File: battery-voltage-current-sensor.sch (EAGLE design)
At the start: 66 parts, among them IC1 ACS758LCB-050B-PFF-T, IC3 ADS1115IDGST, T1 C8545, T2 C8545, T3 C8545, X1 MKDSN1,5/2-5,08

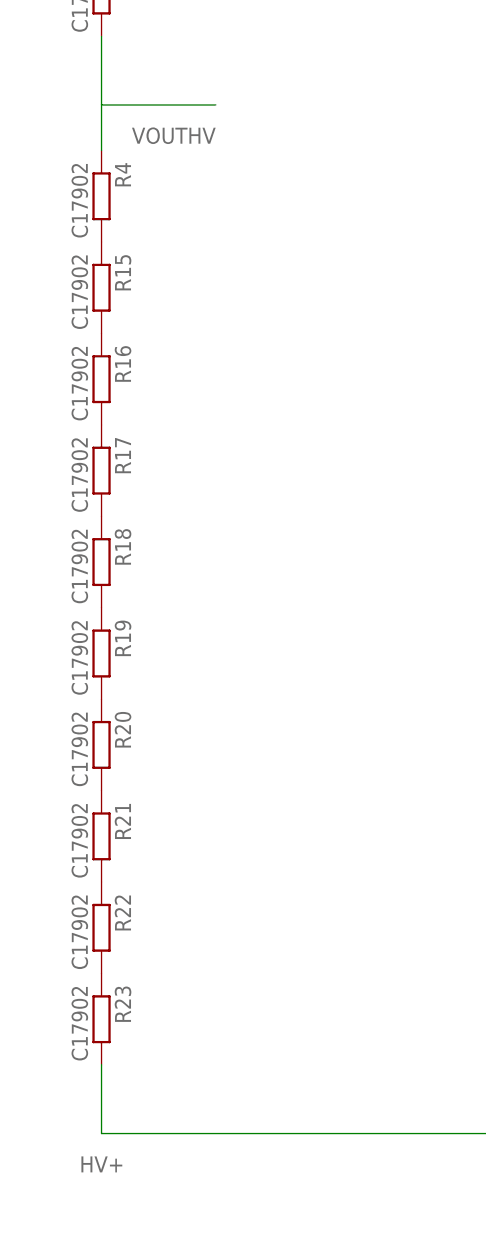
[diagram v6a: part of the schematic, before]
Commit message: voltage measurement resistors changed to 100k
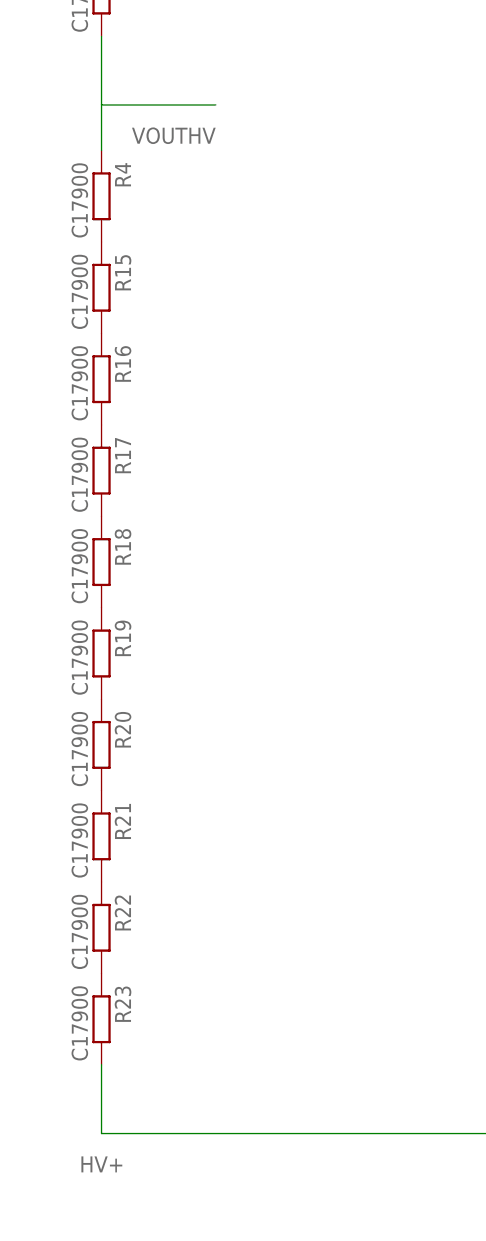
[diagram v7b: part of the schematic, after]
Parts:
- R15, R16, R17, R18, R19, R20, R21, R22, R23, R4: value C17902 -> C17900
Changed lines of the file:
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@@
 <part name="IC1" library="allegro" library_urn="urn:adsk.eagle:library:93" deviceset="ACS758*" device="" package3d_urn="urn:adsk.eagle:package:3449/1" technology="LCB-050B-PFF-T"/>
 <part name="IC3" library="SamacSys_Parts" deviceset="ADS1115IDGST" device=""/>
-<part name="R4" library="rcl" library_urn="urn:adsk.eagle:library:334" deviceset="R-EU_" device="R1206" package3d_urn="urn:adsk.eagle:package:23540/2" value="C17902"/>
-<part name="R15" library="rcl" library_urn="urn:adsk.eagle:library:334" deviceset="R-EU_" device="R1206" package3d_urn="urn:adsk.eagle:package:23540/2" value="C17902"/>
-<part name="R16" library="rcl" library_urn="urn:adsk.eagle:library:334" deviceset="R-EU_" device="R1206" package3d_urn="urn:adsk.eagle:package:23540/2" value="C17902"/>
-<part name="R17" library="rcl" library_urn="urn:adsk.eagle:library:334" deviceset="R-EU_" device="R1206" package3d_urn="urn:adsk.eagle:package:23540/2" value="C17902"/>
-<part name="R18" library="rcl" library_urn="urn:adsk.eagle:library:334" deviceset="R-EU_" device="R1206" package3d_urn="urn:adsk.eagle:package:23540/2" value="C17902"/>
-<part name="R19" library="rcl" library_urn="urn:adsk.eagle:library:334" deviceset="R-EU_" device="R1206" package3d_urn="urn:adsk.eagle:package:23540/2" value="C17902"/>
-<part name="R20" library="rcl" library_urn="urn:adsk.eagle:library:334" deviceset="R-EU_" device="R1206" package3d_urn="urn:adsk.eagle:package:23540/2" value="C17902"/>
-<part name="R21" library="rcl" library_urn="urn:adsk.eagle:library:334" deviceset="R-EU_" device="R1206" package3d_urn="urn:adsk.eagle:package:23540/2" value="C17902"/>
-<part name="R22" library="rcl" library_urn="urn:adsk.eagle:library:334" deviceset="R-EU_" device="R1206" package3d_urn="urn:adsk.eagle:package:23540/2" value="C17902"/>
-<part name="R23" library="rcl" library_urn="urn:adsk.eagle:library:334" deviceset="R-EU_" device="R1206" package3d_urn="urn:adsk.eagle:package:23540/2" value="C17902"/>
+<part name="R4" library="rcl" library_urn="urn:adsk.eagle:library:334" deviceset="R-EU_" device="R1206" package3d_urn="urn:adsk.eagle:package:23540/2" value="C17900"/>
+<part name="R15" library="rcl" library_urn="urn:adsk.eagle:library:334" deviceset="R-EU_" device="R1206" package3d_urn="urn:adsk.eagle:package:23540/2" value="C17900"/>
+<part name="R16" library="rcl" library_urn="urn:adsk.eagle:library:334" deviceset="R-EU_" device="R1206" package3d_urn="urn:adsk.eagle:package:23540/2" value="C17900"/>
+<part name="R17" library="rcl" library_urn="urn:adsk.eagle:library:334" deviceset="R-EU_" device="R1206" package3d_urn="urn:adsk.eagle:package:23540/2" value="C17900"/>
+<part name="R18" library="rcl" library_urn="urn:adsk.eagle:library:334" deviceset="R-EU_" device="R1206" package3d_urn="urn:adsk.eagle:package:23540/2" value="C17900"/>
+<part name="R19" library="rcl" library_urn="urn:adsk.eagle:library:334" deviceset="R-EU_" device="R1206" package3d_urn="urn:adsk.eagle:package:23540/2" value="C17900"/>
+<part name="R20" library="rcl" library_urn="urn:adsk.eagle:library:334" deviceset="R-EU_" device="R1206" package3d_urn="urn:adsk.eagle:package:23540/2" value="C17900"/>
+<part name="R21" library="rcl" library_urn="urn:adsk.eagle:library:334" deviceset="R-EU_" device="R1206" package3d_urn="urn:adsk.eagle:package:23540/2" value="C17900"/>
+<part name="R22" library="rcl" library_urn="urn:adsk.eagle:library:334" deviceset="R-EU_" device="R1206" package3d_urn="urn:adsk.eagle:package:23540/2" value="C17900"/>
+<part name="R23" library="rcl" library_urn="urn:adsk.eagle:library:334" deviceset="R-EU_" device="R1206" package3d_urn="urn:adsk.eagle:package:23540/2" value="C17900"/>
 <part name="R24" library="rcl" library_urn="urn:adsk.eagle:library:334" deviceset="R-EU_" device="R0805" package3d_urn="urn:adsk.eagle:package:23553/2" value="C17772"/>
 <part name="C4" library="rcl" library_urn="urn:adsk.eagle:library:334" deviceset="C-EU" device="C0805" package3d_urn="urn:adsk.eagle:package:23617/2" value="100nF"/>

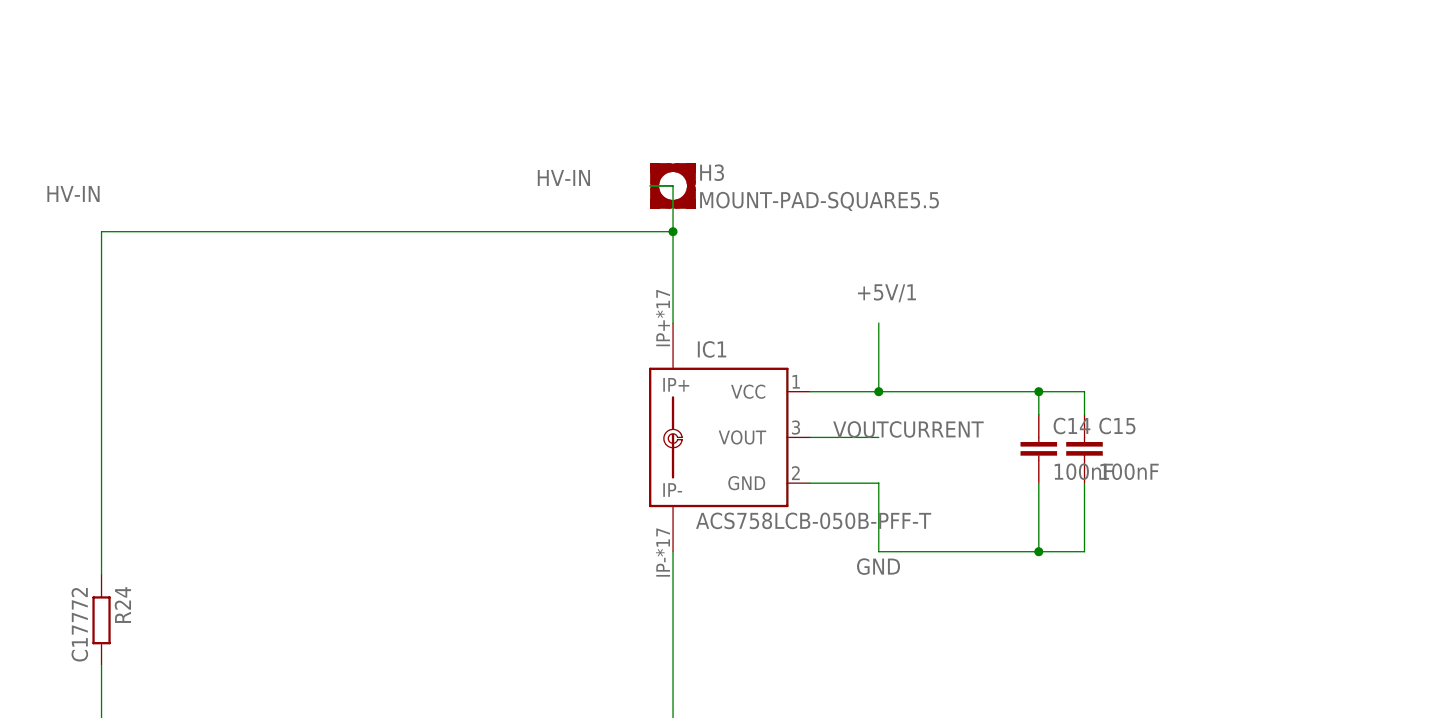
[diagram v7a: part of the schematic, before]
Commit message: 1000V DCDC position corrected
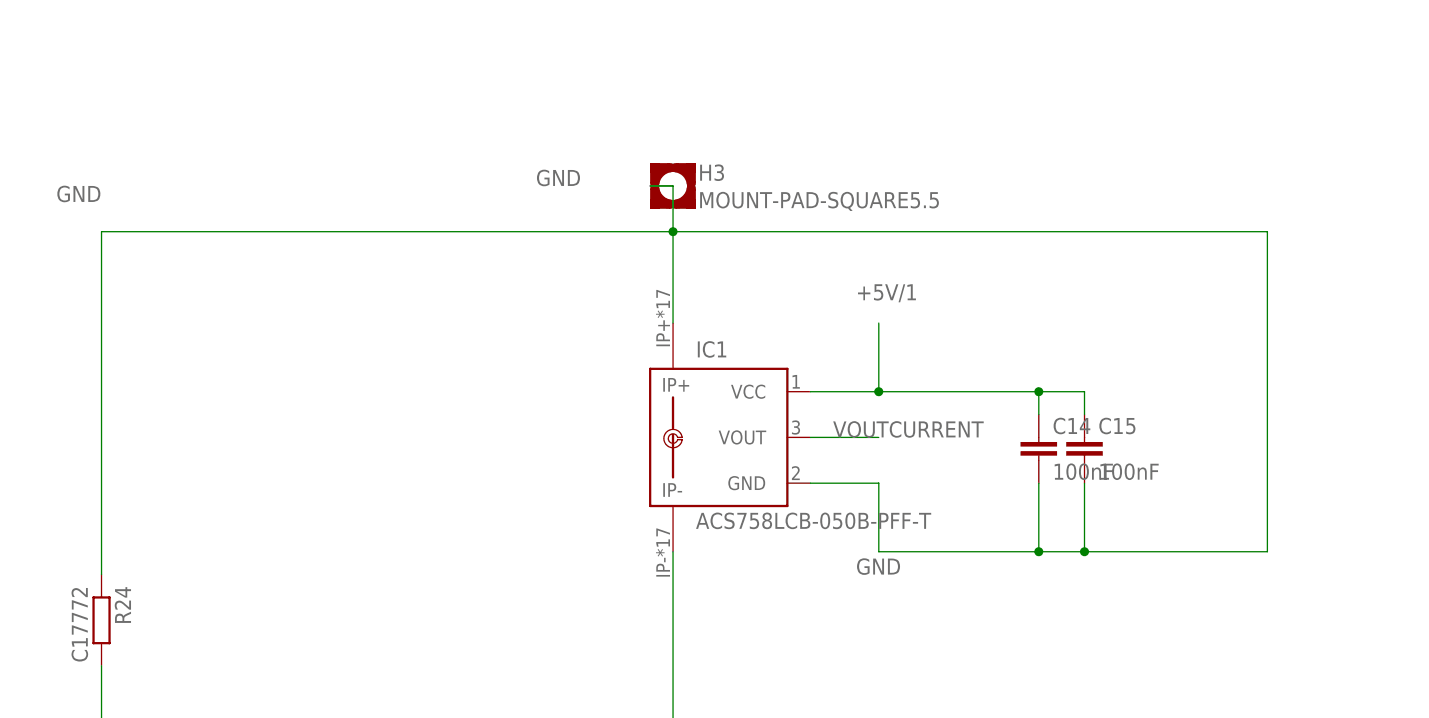
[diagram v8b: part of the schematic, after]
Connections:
- removed net HV-IN: H3.MOUNT, IC1.IP+, R24.1
- net GND: now also H3.MOUNT, IC1.IP+, R24.1
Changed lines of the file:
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@@
-</segment>
-<segment>
-<pinref part="IC1" gate="G$1" pin="GND"/>
-<wire x1="15.24" y1="162.56" x2="22.86" y2="162.56" width="0.1524" layer="91"/>
-<wire x1="22.86" y1="162.56" x2="22.86" y2="154.94" width="0.1524" layer="91"/>
-<label x="20.32" y="152.4" size="1.778" layer="95"/>
-<pinref part="C14" gate="G$1" pin="2"/>
-<wire x1="22.86" y1="154.94" x2="40.64" y2="154.94" width="0.1524" layer="91"/>
-<wire x1="40.64" y1="154.94" x2="40.64" y2="162.56" width="0.1524" layer="91"/>
-<pinref part="C15" gate="G$1" pin="2"/>
-<wire x1="40.64" y1="154.94" x2="45.72" y2="154.94" width="0.1524" layer="91"/>
-<wire x1="45.72" y1="154.94" x2="45.72" y2="162.56" width="0.1524" layer="91"/>
-<junction x="40.64" y="154.94"/>
 </segment>
 <segment>
@@
 <label x="134.62" y="45.72" size="1.778" layer="95"/>
 </segment>
+<segment>
+<pinref part="H3" gate="G$1" pin="MOUNT"/>
+<pinref part="IC1" gate="G$1" pin="IP+"/>
+<wire x1="-2.54" y1="195.58" x2="0" y2="195.58" width="0.1524" layer="91"/>
+<wire x1="0" y1="195.58" x2="0" y2="190.5" width="0.1524" layer="91"/>
+<label x="-15.24" y="195.58" size="1.778" layer="95"/>
+<wire x1="0" y1="190.5" x2="0" y2="180.34" width="0.1524" layer="91"/>
+<wire x1="-63.5" y1="190.5" x2="0" y2="190.5" width="0.1524" layer="91"/>
+<pinref part="R24" gate="G$1" pin="1"/>
+<wire x1="-63.5" y1="152.4" x2="-63.5" y2="190.5" width="0.1524" layer="91"/>
+<label x="-63.5" y="195.58" size="1.778" layer="95" rot="R180"/>
+<junction x="0" y="190.5"/>
+<wire x1="0" y1="190.5" x2="66.04" y2="190.5" width="0.1524" layer="91"/>
+<wire x1="66.04" y1="190.5" x2="66.04" y2="154.94" width="0.1524" layer="91"/>
+<pinref part="IC1" gate="G$1" pin="GND"/>
+<wire x1="15.24" y1="162.56" x2="22.86" y2="162.56" width="0.1524" layer="91"/>
+<wire x1="22.86" y1="162.56" x2="22.86" y2="154.94" width="0.1524" layer="91"/>
+<label x="20.32" y="152.4" size="1.778" layer="95"/>
+<pinref part="C14" gate="G$1" pin="2"/>
+<wire x1="22.86" y1="154.94" x2="40.64" y2="154.94" width="0.1524" layer="91"/>
+<wire x1="40.64" y1="154.94" x2="40.64" y2="162.56" width="0.1524" layer="91"/>
+<pinref part="C15" gate="G$1" pin="2"/>
+<wire x1="40.64" y1="154.94" x2="45.72" y2="154.94" width="0.1524" layer="91"/>
+<wire x1="45.72" y1="154.94" x2="45.72" y2="162.56" width="0.1524" layer="91"/>
+<junction x="40.64" y="154.94"/>
+<wire x1="66.04" y1="154.94" x2="45.72" y2="154.94" width="0.1524" layer="91"/>
+<junction x="45.72" y="154.94"/>
+</segment>
 </net>
 <net name="+5V/1" class="0">
@@
 </segment>
 </net>
-<net name="HV-IN" class="1">
-<segment>
-<pinref part="H3" gate="G$1" pin="MOUNT"/>
-<pinref part="IC1" gate="G$1" pin="IP+"/>
-<wire x1="-2.54" y1="195.58" x2="0" y2="195.58" width="0.1524" layer="91"/>
-<wire x1="0" y1="195.58" x2="0" y2="190.5" width="0.1524" layer="91"/>
-<label x="-15.24" y="195.58" size="1.778" layer="95"/>
-<wire x1="0" y1="190.5" x2="0" y2="180.34" width="0.1524" layer="91"/>
-<wire x1="-63.5" y1="190.5" x2="0" y2="190.5" width="0.1524" layer="91"/>
-<pinref part="R24" gate="G$1" pin="1"/>
-<wire x1="-63.5" y1="152.4" x2="-63.5" y2="190.5" width="0.1524" layer="91"/>
-<label x="-63.5" y="195.58" size="1.778" layer="95" rot="R180"/>
-<junction x="0" y="190.5"/>
-</segment>
-</net>
